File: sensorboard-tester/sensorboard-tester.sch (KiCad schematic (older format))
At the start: 13 parts, among them J0 Power, J1 USB_B, J2 LEDCurrentProbe, U1 Opamp_Dual_Generic

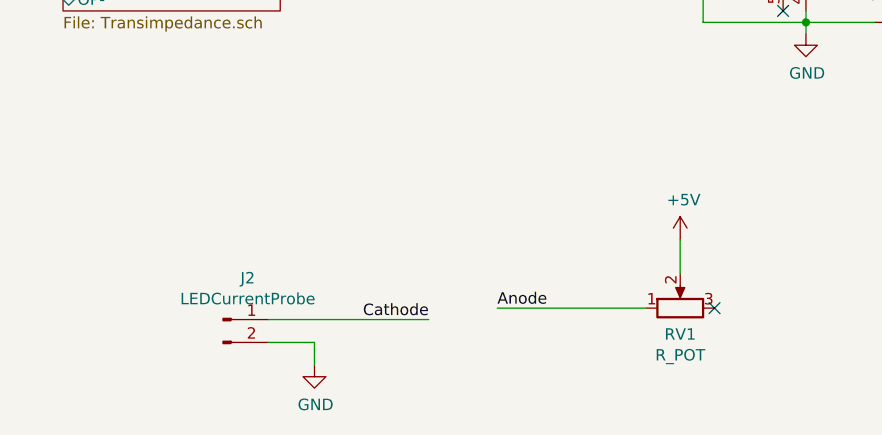
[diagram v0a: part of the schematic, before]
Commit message: Cleanup and reconcile the headers. Switch to SOT23 regulators for both.
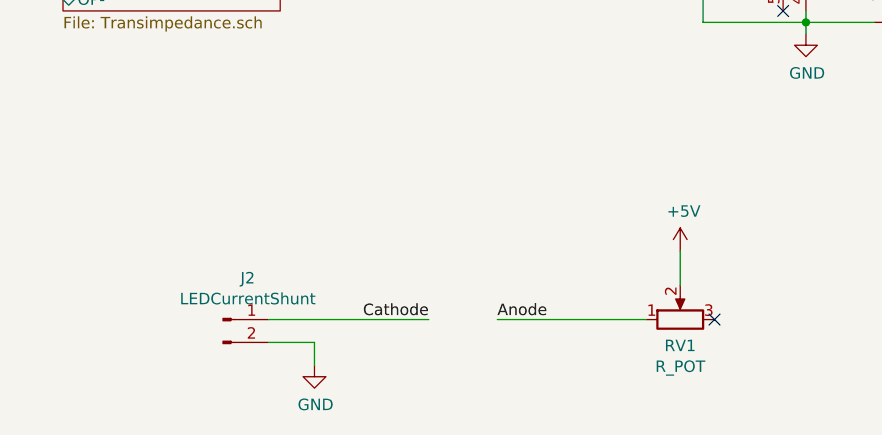
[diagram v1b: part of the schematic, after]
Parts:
- J2: value LEDCurrentProbe -> LEDCurrentShunt
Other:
- moved on the sheet: RV1
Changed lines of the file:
@@
 AR Path="/5FC7E376" Ref="J2"  Part="1"
 F 0 "J2" H 6358 4931 50  0000 C CNN
-F 1 "LEDCurrentProbe" H 6358 4840 50  0000 C CNN
+F 1 "LEDCurrentShunt" H 6358 4840 50  0000 C CNN
 F 2 "Pin_Headers:Pin_Header_Straight_1x02_Pitch2.54mm" H 6250 4750 50  0001 C CNN
 F 3 "~" H 6250 4750 50  0001 C CNN
@@
 L Device:R_POT RV?
 U 1 1 5FC7E386
-P 8250 4700
+P 8250 4750
 AR Path="/5FC34DE6/5FC7E386" Ref="RV?"  Part="1"
 AR Path="/5FC7E386" Ref="RV1"  Part="1"
-F 0 "RV1" V 8135 4700 50  0000 C CNN
-F 1 "R_POT" V 8044 4700 50  0000 C CNN
-F 2 "Potentiometers:Potentiometer_WirePads_Small" H 8250 4700 50  0001 C CNN
-F 3 "~" H 8250 4700 50  0001 C CNN
-	1    8250 4700
+F 0 "RV1" V 8135 4750 50  0000 C CNN
+F 1 "R_POT" V 8044 4750 50  0000 C CNN
+F 2 "Potentiometers:Potentiometer_WirePads_Small" H 8250 4750 50  0001 C CNN
+F 3 "~" H 8250 4750 50  0001 C CNN
+	1    8250 4750
 	0    -1   -1   0
 $EndComp
@@
 L power:+5V #PWR?
 U 1 1 5FC7E38C
-P 8250 4400
+P 8250 4450
 AR Path="/5FC34DE6/5FC7E38C" Ref="#PWR?"  Part="1"
 AR Path="/5FC7E38C" Ref="#PWR0102"  Part="1"
-F 0 "#PWR0102" H 8250 4250 50  0001 C CNN
-F 1 "+5V" H 8265 4573 50  0000 C CNN
-F 2 "" H 8250 4400 50  0001 C CNN
-F 3 "" H 8250 4400 50  0001 C CNN
-	1    8250 4400
+F 0 "#PWR0102" H 8250 4300 50  0001 C CNN
+F 1 "+5V" H 8265 4623 50  0000 C CNN
+F 2 "" H 8250 4450 50  0001 C CNN
+F 3 "" H 8250 4450 50  0001 C CNN
+	1    8250 4450
 	1    0    0    -1
 $EndComp
-NoConn ~ 8400 4700
-Text Label 7450 4700 0    50   ~ 0
+NoConn ~ 8400 4750
+Text Label 7450 4750 0    50   ~ 0
 Anode
 Wire Wire Line
@@
 Cathode
 Wire Wire Line
-	7450 4700 8100 4700
+	7450 4750 8100 4750
 Wire Wire Line
-	8250 4400 8250 4550
+	8250 4450 8250 4600
 $Comp
 L Connector:TestPoint_Probe TP?
